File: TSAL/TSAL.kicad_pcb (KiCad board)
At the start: 2 copper layers, 42 parts, among them J1 Conn_02x03_Counter_Clockwise, J2 Conn_01x02, J4 Conn_02x01, U1 LM358, U2 4002, U3 74HC00, U4 4N35, U5 74HC21, U6 74HC7014, U7 LM7805_TO220, U8 LM339, U9 LM339

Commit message: CREATE TSAL PCBs
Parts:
- removed R23: 22K, Resistor_SMD:R_0603_1608Metric_Pad0.98x0.95mm_HandSolder
- removed R24: 33K, Resistor_SMD:R_0603_1608Metric_Pad0.98x0.95mm_HandSolder
- added C3: 100uF, Capacitor_SMD:C_Elec_6.3x7.7, F.Cu at (129.4, 81.9)
- added C4: 0.1uF, Capacitor_SMD:C_0603_1608Metric_Pad1.08x0.95mm_HandSolder, F.Cu at (112.4, 82.6)
- added D2: GRN, LED_SMD:LED_0805_2012Metric_Pad1.15x1.40mm_HandSolder, F.Cu at (141.8, 58.2)
- added G***: LOGO, LOGO, F.Cu at (146.0, 61.2)
- added J3: Conn_02x01, Connector_Molex:Molex_Micro-Fit_3.0_43045-0212_2x01_P3.00mm_Vertical, F.Cu at (139.9, 63.4)
- added Q1: BSS138, Package_TO_SOT_SMD:SOT-23, F.Cu at (112.4, 75.2)
- added Q2: BSS138, Package_TO_SOT_SMD:SOT-23, F.Cu at (128.2, 73.0)
- added Q3: AO3401A, Package_TO_SOT_SMD:SOT-23, F.Cu at (133.4, 70.5)
- added R14: 12K, Resistor_SMD:R_0603_1608Metric_Pad0.98x0.95mm_HandSolder, F.Cu at (86.8, 59.9)
- added R15: 7.5K, Resistor_SMD:R_0603_1608Metric_Pad0.98x0.95mm_HandSolder, F.Cu at (133.2, 74.4)
- added R19: 10K, Resistor_SMD:R_0603_1608Metric_Pad0.98x0.95mm_HandSolder, F.Cu at (112.4, 79.1)
- added R20: 10K, Resistor_SMD:R_0603_1608Metric_Pad0.98x0.95mm_HandSolder, F.Cu at (112.4, 80.8)
- added R21: 2k2, Resistor_SMD:R_0603_1608Metric_Pad0.98x0.95mm_HandSolder, F.Cu at (137.7, 58.2)
- added REF**: Symbol_HighVoltage_Triangle_6x6mm_Copper, Symbol:Symbol_HighVoltage_Triangle_6x6mm_Copper, F.Cu at (63.1, 48.2)
- added U10: 74HC74, Package_DIP:DIP-14_W7.62mm, F.Cu at (124.9, 50.6)
- added e1: R_Potentiometer_Trim, Potentiometer_THT:Potentiometer_Bourns_3386F_Vertical, F.Cu at (137.7, 79.2)
- J2: footprint Connector_Molex:Molex_Micro-Fit_3.0_43650-0215_1x02_P3.00mm_Vertical -> Connector_Molex:Molex_Mini-Fit_Jr_5566-02A_2x01_P4.20mm_Vertical
- R13: value 12K -> 10K
- R16: value 1K -> 500; footprint Resistor_SMD:R_0805_2012Metric_Pad1.20x1.40mm_HandSolder -> Resistor_SMD:R_0603_1608Metric_Pad0.98x0.95mm_HandSolder
- U2: value 4002 -> 74HC27; footprint Package_DIP:DIP-16_W7.62mm -> Package_SO:SOIC-14_3.9x8.7mm_P1.27mm
- U3: value 74HC00 -> 74HC20
- U5: value 74HC21 -> 74HC08; footprint Package_SO:SOIC-14_3.9x8.7mm_P1.27mm -> Package_DIP:DIP-14_W7.62mm
- U6: value 74HC7014 -> 74HC86; footprint Package_SO:SOIC-14_3.9x8.7mm_P1.27mm -> Package_DIP:DIP-14_W7.62mm
- U8, U9: footprint Package_SO:SOIC-14_3.9x8.7mm_P1.27mm -> Package_DIP:DIP-14_W7.62mm
- moved J4 78.6 mm to (139.6, 47.3)
- moved U2 73.8 mm to (106.3, 75.5)
- moved U8 67.3 mm to (116.2, 70.4)
- moved H3 64.9 mm to (143.7, 34.6)
- moved H4 57.8 mm to (143.7, 85.2)
- moved U6 50.2 mm to (100.2, 86.1), turned to 180 degrees
- moved R33 48.6 mm to (63.1, 65.5), turned to -90 degrees
- moved U1 45.3 mm to (68.3, 62.7)
- moved U9 45.0 mm to (121.0, 66.0), turned to 180 degrees
- moved J1 44.2 mm to (123.8, 37.8)
- moved U7 38.3 mm to (87.8, 38.5), turned to -90 degrees
- moved U5 38.0 mm to (102.6, 50.6)
- moved R34 37.7 mm to (73.7, 65.4), turned to 90 degrees
- moved R35 36.9 mm to (73.7, 61.7), turned to 90 degrees
- moved H2 35.9 mm to (62.3, 85.2)
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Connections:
- J1 pad 1: /AIR+ -> /Precharge
- J1 pad 2: /AIR+_Int -> /PreCh_Int
- J1 pad 3: /AIR-_Int -> /AIR-
- J1 pad 4: /AIR- -> /AIR-_Int
- J1 pad 5: /PreCh_Int -> /AIR+_Int
- J1 pad 6: /Precharge -> /AIR+
- R13 pad 1: GLV+ -> /5V
- U2 pad 1: /GRN_OK -> Net-(U2-Pad1)
- U2 pad 12: unconnected-(U2-Pad12) -> /PLUASBL_CHK
- U2 pad 13: unconnected-(U2-Pad13) -> Net-(U2-Pad13)_1
- U2 pad 2: /AIR+_TSAL -> Net-(U2-Pad2)
- U2 pad 3: /AIR-_TSAL -> (no net)
- U2 pad 4: /Precharge_TSAL -> (no net)
- U2 pad 5: /VHI<60V -> (no net)
- U3 pad 1: /PreCh_Int -> /AIR+
- U3 pad 10: /AIR- -> unconnected-(U3-Pad10)
- U3 pad 11: unconnected-(U3-Pad11) -> (no net)
- U3 pad 2: /Precharge -> /AIR-
- U3 pad 3: unconnected-(U3-Pad3) -> (no net)
- U3 pad 4: /AIR+_Int -> /Precharge
- U3 pad 5: /AIR+ -> /~{VHI<60V}
- U3 pad 6: unconnected-(U3-Pad6) -> /GRN_OK
- U3 pad 8: (no net) -> unconnected-(U3-Pad8)
- U3 pad 9: /AIR-_Int -> unconnected-(U3-Pad9)
- U4 pad 4: Net-(R24-Pad1) -> GLV-
- U4 pad 5: GLV+ -> /~{VHI<60V}
- U5 pad 1: (no net) -> /GRN_OK
- U5 pad 10: (no net) -> Net-(Q2-G)
- U5 pad 11: (no net) -> unconnected-(U5-Pad11)
- U5 pad 12: (no net) -> unconnected-(U5-Pad12)
- U5 pad 13: (no net) -> unconnected-(U5-Pad13)
- U5 pad 2: (no net) -> /SCS_Compliance
- U5 pad 3: (no net) -> Net-(U5-Pad3)
- U5 pad 4: (no net) -> /GRN_LIGHT
- U5 pad 5: (no net) -> Net-(U5-Pad3)
- U5 pad 6: (no net) -> /PLUASBL_CHK
- U5 pad 8: (no net) -> /GRN_LIGHT
- U5 pad 9: (no net) -> Net-(U10A-Q)
- U6 pad 1: (no net) -> /PreCh_Int
- U6 pad 10: (no net) -> /AIR-
- U6 pad 11: (no net) -> unconnected-(U6-Pad11)
- U6 pad 12: (no net) -> unconnected-(U6-Pad12)
- U6 pad 13: (no net) -> unconnected-(U6-Pad13)
- U6 pad 2: (no net) -> /Precharge
- U6 pad 3: (no net) -> Net-(U2-Pad1)
- U6 pad 4: (no net) -> /AIR+_Int
- U6 pad 5: (no net) -> /AIR+
- U6 pad 6: (no net) -> Net-(U2-Pad2)
- U6 pad 8: (no net) -> Net-(U2-Pad13)_1
- U6 pad 9: (no net) -> /AIR-_Int
- U8 pad 3: GLV+ -> /5V
- U9 pad 3: GLV+ -> /5V
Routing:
- net /5V: track 0.00 -> 165.4 mm, vias 0 -> 1
- net GLV+: track 0.00 -> 129.3 mm
- net /Precharge: track 0.00 -> 100.1 mm, vias 0 -> 2
- net /PreCh_Int: track 0.00 -> 92.3 mm, vias 0 -> 4
- net /AIR+_Int: track 0.00 -> 77.4 mm
- net /AIR-: track 0.00 -> 71.0 mm
- net /AIR+: track 0.00 -> 70.2 mm
- net /AIR-_Int: track 0.00 -> 57.7 mm, vias 0 -> 2
- net /.25V: track 0.00 -> 54.7 mm, vias 0 -> 3
- net /SCS_Compliance: track 0.00 -> 43.0 mm
- net Net-(U10A-~{S}): track 0.00 -> 33.8 mm, vias 0 -> 3
- net Net-(Q1-D): track 0.00 -> 32.2 mm, vias 0 -> 4
- net Net-(U2-Pad13)_1: track 0.00 -> 24.7 mm
- net Net-(Q2-G): track 0.00 -> 24.0 mm, vias 0 -> 1
- net /5V+_Iso: track 0.00 -> 23.7 mm
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- added copper zone on B.Cu, net GLV-
- added copper zone on F.Cu, net GLV-
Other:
- board outline added: 89.4 x 58.2 mm
- board text added: "0.2000 mm / 0.2000 mm"
- board text added: "0.3000 mm"
- board text added: "1.6000 mm"
- board text added: "2"
- board text added: "89.3550 mm x 58.1550 mm"
- board text added: "BOARD CHARACTERISTICS"
- board text added: "Board Thickness:"
- board text added: "Board overall dimensions:"
- board text added: "Castellated pads:"
- board text added: "Copper Finish:"
- board text added: "Copper Layer Count:"
- board text added: "Edge card connectors:"
- board text added: "HAL SnPb"
- board text added: "HIGH VOLTAGE"
- board text added: "HV"
- board text added: "IT'S SAFE!"
- board text added: "Impedance Control:"
- board text added: "LV"
- board text added: "Min hole diameter:"
- board text added: "Min track/spacing:"
- board text added: "No"
- board text added: "PS1"
- board text added: "Plated Board Edge:"
- board text added: "v1.0"

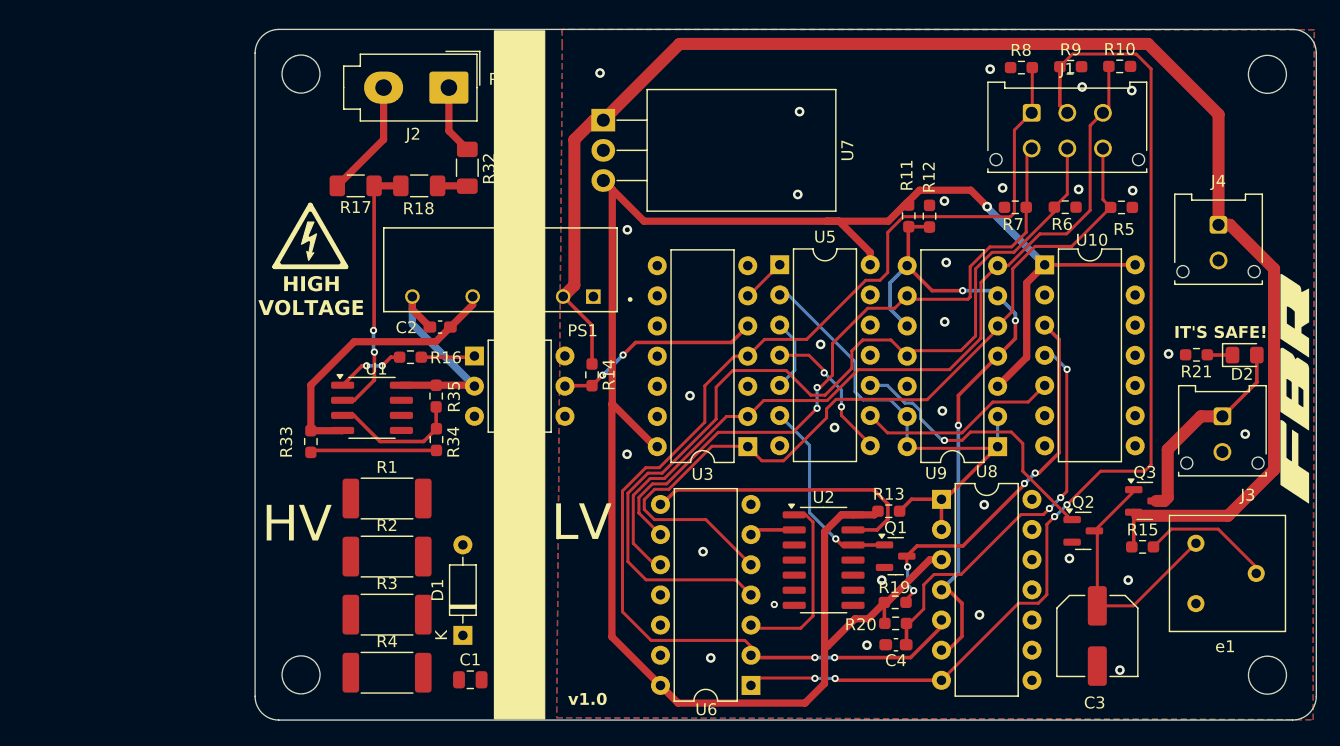
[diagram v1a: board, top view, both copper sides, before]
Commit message: ADD 12x12 logo
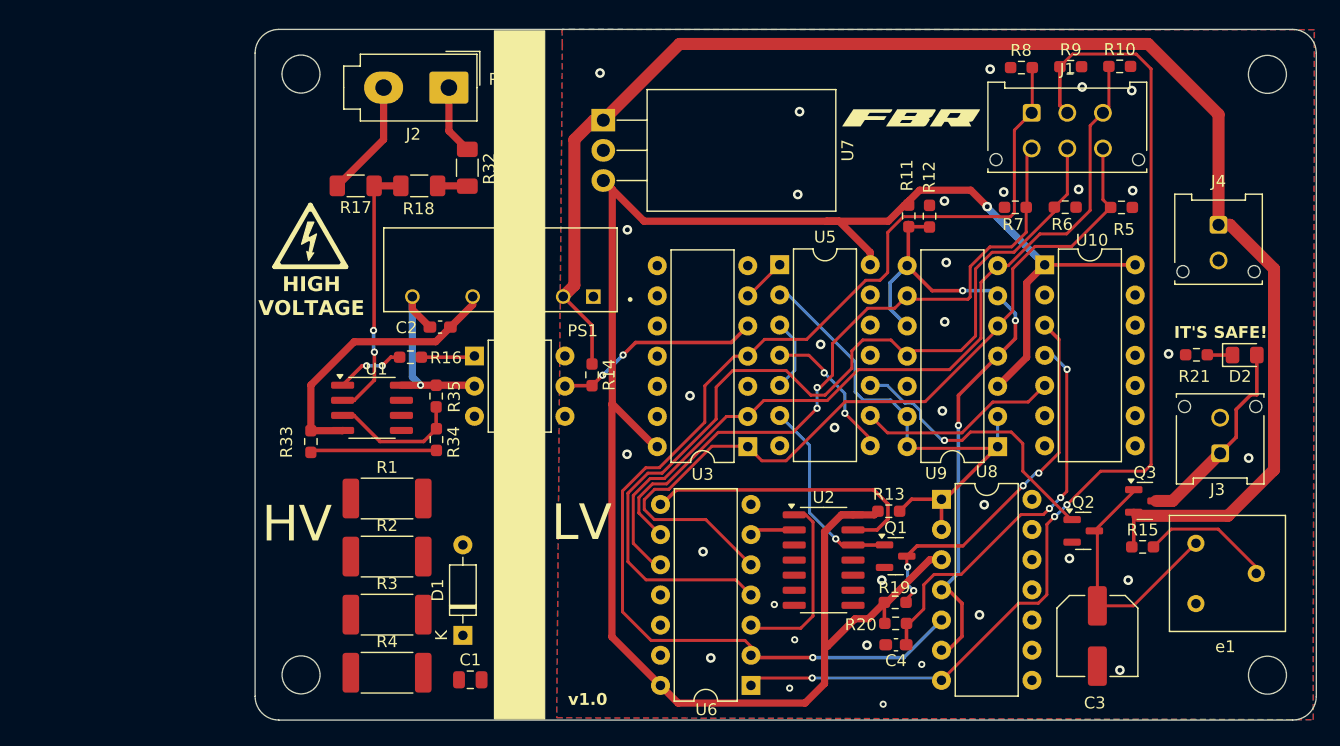
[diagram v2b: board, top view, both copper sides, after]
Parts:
- moved G*** 39.7 mm to (113.6, 38.2), turned to 0 degrees
- moved J3 3.12 mm to (139.7, 66.5), turned to 180 degrees
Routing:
- net /5V-_Iso: track 19.1 -> 17.1 mm, vias 0 -> 1
- net /PreCh_Int: track 92.3 -> 91.7 mm, vias 4 -> 3
- net /Precharge: track 100.1 -> 100.3 mm, vias 2 -> 1
- net GLV-: vias 30 -> 34

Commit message: v1.0.1
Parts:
- moved J1 7.17 mm to (129.9, 41.7), turned to 180 degrees
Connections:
- J1 pad 1: /Precharge -> /AIR-
- J1 pad 3: /AIR- -> /Precharge
- J1 pad 4: /AIR-_Int -> /AIR+
- J1 pad 6: /AIR+ -> /AIR-_Int
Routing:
- net /PreCh_Int: track 91.7 -> 96.0 mm
- net /AIR+_Int: track 77.4 -> 80.3 mm
- net /AIR+: track 69.7 -> 72.4 mm
- net /AIR-_Int: track 57.7 -> 59.4 mm
- net /AIR-: track 71.0 -> 72.3 mm
- net /Precharge: track 100.3 -> 101.2 mm
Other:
- board text added: "AIR+"
- board text added: "AIR+_Int"
- board text added: "AIR-"
- board text added: "AIR-_Int"
- board text added: "PreChg"
- board text added: "PreInt"

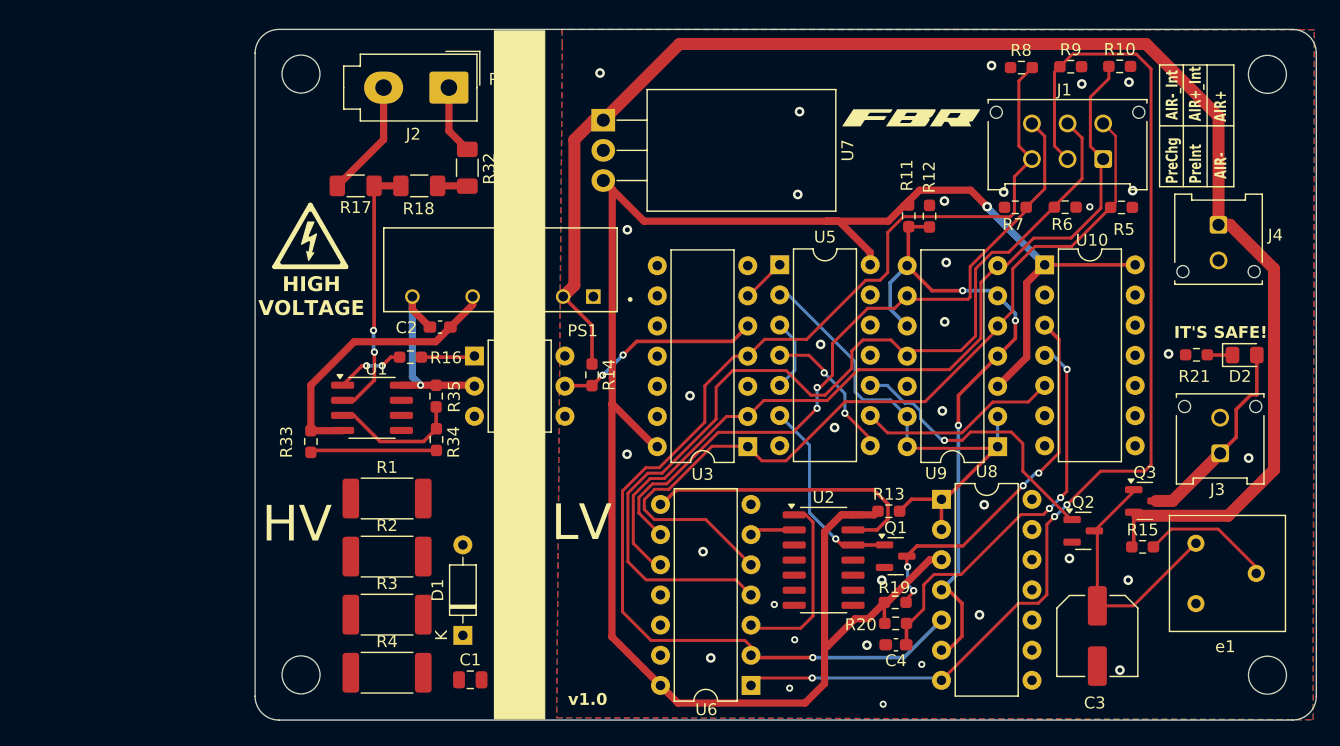
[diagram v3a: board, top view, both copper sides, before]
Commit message: Modify TSAL PCB and use relative paths for libraries
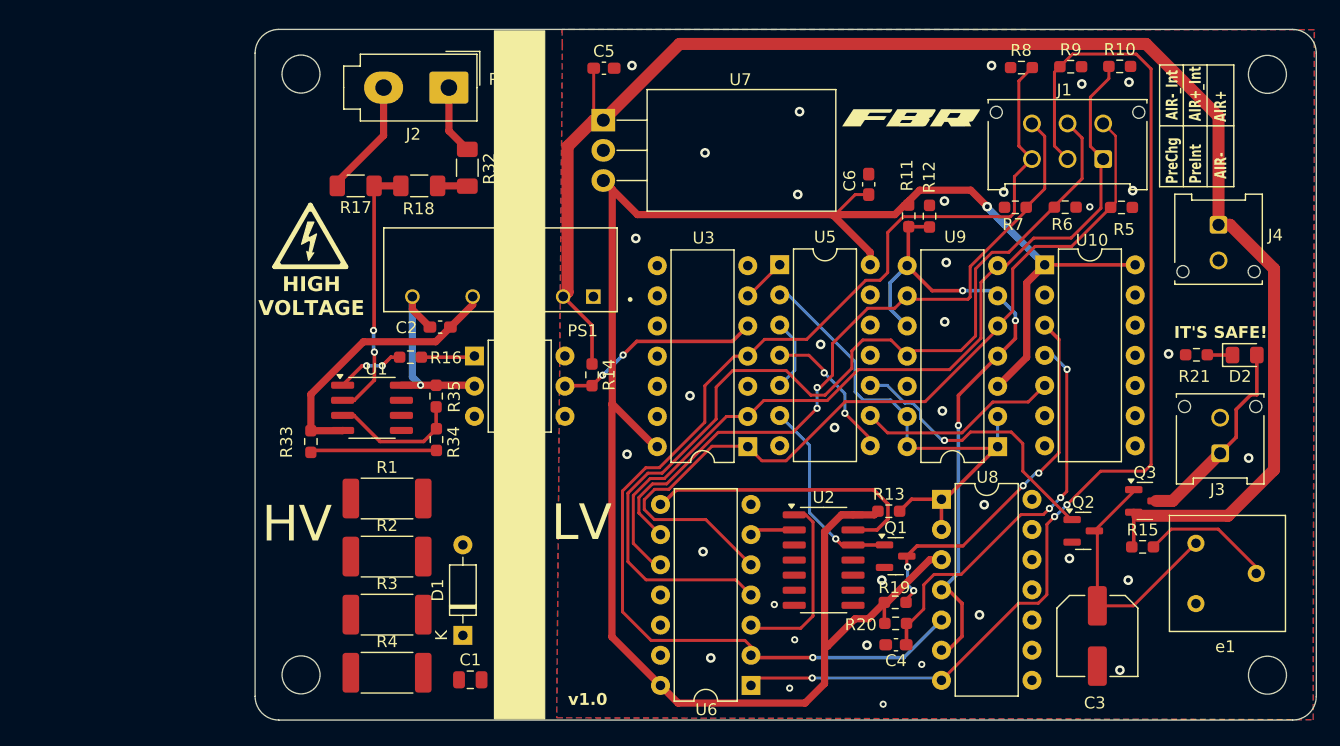
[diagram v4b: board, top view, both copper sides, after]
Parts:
- added C5: .33uF, Capacitor_SMD:C_0603_1608Metric_Pad1.08x0.95mm_HandSolder, F.Cu at (87.8, 34.1)
- added C6: 0.1uF, Capacitor_SMD:C_0603_1608Metric_Pad1.08x0.95mm_HandSolder, F.Cu at (110.1, 43.9)
- R11: value 19.1K -> 100K
- R12: value 1K -> 5.1K
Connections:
- U5 pad 11: unconnected-(U5-Pad11) -> (no net)
- U5 pad 12: unconnected-(U5-Pad12) -> (no net)
- U5 pad 13: unconnected-(U5-Pad13) -> (no net)
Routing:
- net GLV+: track 129.1 -> 133.9 mm
- net /5V: track 165.4 -> 168.8 mm
- net GLV-: vias 34 -> 35

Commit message: minor changes
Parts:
- removed C1: 0.1 uF, Capacitor_SMD:C_0805_2012Metric
- removed D1: 2.4V, Diode_THT:D_DO-35_SOD27_P7.62mm_Horizontal
- removed R1, R2: 5.6K, Resistor_SMD:R_2512_6332Metric_Pad1.40x3.35mm_HandSolder
- removed R3: 6.8K, Resistor_SMD:R_2512_6332Metric_Pad1.40x3.35mm_HandSolder
- removed R4: 2.7K, Resistor_SMD:R_2512_6332Metric_Pad1.40x3.35mm_HandSolder
- added R22: 500K, Resistor_SMD:R_0603_1608Metric_Pad0.98x0.95mm_HandSolder, F.Cu at (112.4, 84.4)
- R16: value 500 -> 390
- moved C6 24.8 mm to (87.8, 33.0), turned to 180 degrees
- moved R32 10.8 mm to (68.6, 35.0)
- moved R33 9.80 mm to (72.9, 64.4), turned to 180 degrees
- moved U1 7.20 mm to (72.3, 68.7)
- moved REF** 5.52 mm to (64.3, 42.8)
- moved R18 5.18 mm to (68.6, 40.3), turned to 90 degrees
- moved R17 3.49 mm to (70.2, 45.3), turned to 0 degrees
- moved R34 2.78 mm to (72.9, 62.7), turned to 180 degrees
- moved R16 2.40 mm to (73.8, 57.7)
- moved H2 2.05 mm to (64.4, 85.2)
- moved H1 2.05 mm to (64.4, 34.6)
- moved J2 1.37 mm to (74.0, 34.6), turned to 0 degrees
- moved R35 1.08 mm to (72.9, 61.0), turned to 0 degrees
- moved C5 0.58 mm to (87.9, 34.7)
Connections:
- net HV+ renamed /HV+
- U10 pad 10: unconnected-(U10B-~{S}-Pad10) -> (no net)
- U10 pad 11: unconnected-(U10B-C-Pad11) -> (no net)
- U10 pad 12: unconnected-(U10B-D-Pad12) -> (no net)
- U10 pad 13: unconnected-(U10B-~{R}-Pad13) -> (no net)
- U10 pad 8: unconnected-(U10B-~{Q}-Pad8) -> (no net)
- U10 pad 9: unconnected-(U10B-Q-Pad9) -> (no net)
- U2 pad 10: unconnected-(U2-Pad10) -> (no net)
- U2 pad 11: unconnected-(U2-Pad11) -> (no net)
- U2 pad 9: unconnected-(U2-Pad9) -> (no net)
- U3 pad 10: unconnected-(U3-Pad10) -> (no net)
- U3 pad 12: unconnected-(U3-Pad12) -> (no net)
- U3 pad 13: unconnected-(U3-Pad13) -> (no net)
- U3 pad 8: unconnected-(U3-Pad8) -> (no net)
- U3 pad 9: unconnected-(U3-Pad9) -> (no net)
- U6 pad 11: unconnected-(U6-Pad11) -> (no net)
- U6 pad 12: unconnected-(U6-Pad12) -> (no net)
- U6 pad 13: unconnected-(U6-Pad13) -> (no net)
- U8 pad 10: unconnected-(U8C---Pad10) -> (no net)
- U8 pad 11: unconnected-(U8C-+-Pad11) -> (no net)
- U8 pad 13: unconnected-(U8-Pad13) -> (no net)
- U8 pad 14: unconnected-(U8-Pad14) -> (no net)
- U8 pad 8: unconnected-(U8D---Pad8) -> (no net)
- U8 pad 9: unconnected-(U8D-+-Pad9) -> (no net)
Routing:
- net /5V-_Iso: track 17.1 -> 3.68 mm, vias 1 -> 2
- net /5V: track 168.8 -> 179.5 mm, vias 1 -> 2
- net Net-(R33-Pad2): track 10.7 -> 2.57 mm
- net Net-(U1A--): track 22.9 -> 28.5 mm, vias 2 -> 0
- net Net-(R16-Pad1): track 5.78 -> 11.0 mm, vias 2 -> 0
- net /HV+: track 9.89 -> 6.16 mm
- net /AIR+_Int: track 80.3 -> 77.3 mm
- net /VHI<60V: track 4.83 -> 2.45 mm
- net Net-(U10A-~{S}): track 33.8 -> 35.6 mm
- net /5V+_Iso: track 23.2 -> 24.4 mm, vias 0 -> 1
- net Net-(Q2-G): track 24.0 -> 25.0 mm
- net Net-(Q2-D): track 21.7 -> 22.6 mm
- net /Precharge: track 101.2 -> 100.6 mm
- net /AIR-_Int: track 59.4 -> 59.9 mm
- net GLV-: vias 35 -> 70
- added copper zone on B.Cu, net /5V-_Iso
- added copper zone on F.Cu, net /5V-_Iso
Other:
- board size 89.4 x 58.2 mm -> 87.6 x 58.1 mm
- board text added: "87.6300 mm x 58.1200 mm"
- board text added: "v1.2"
- board text removed: "89.3550 mm x 58.1550 mm"
- board text removed: "v1.0"

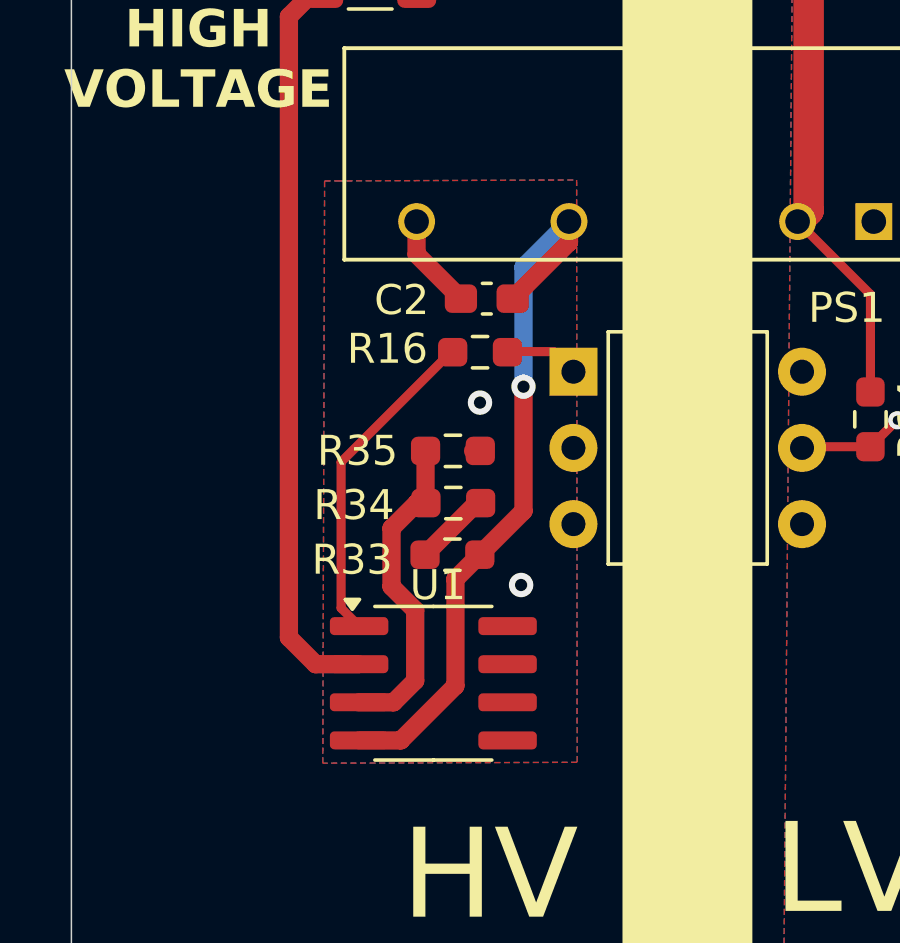
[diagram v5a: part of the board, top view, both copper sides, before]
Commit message: Updated to KiCad v9
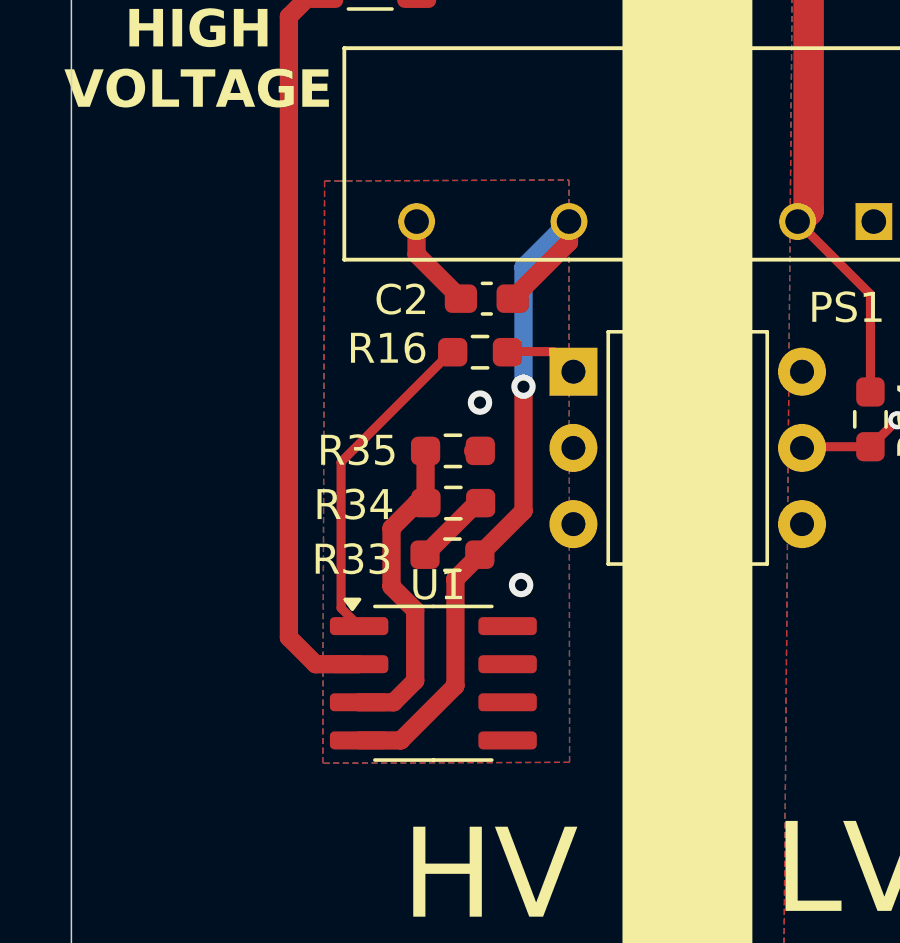
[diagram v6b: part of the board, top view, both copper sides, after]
